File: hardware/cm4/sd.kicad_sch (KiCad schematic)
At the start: 5 parts, among them J13 microSD, U11 AP22804AW5

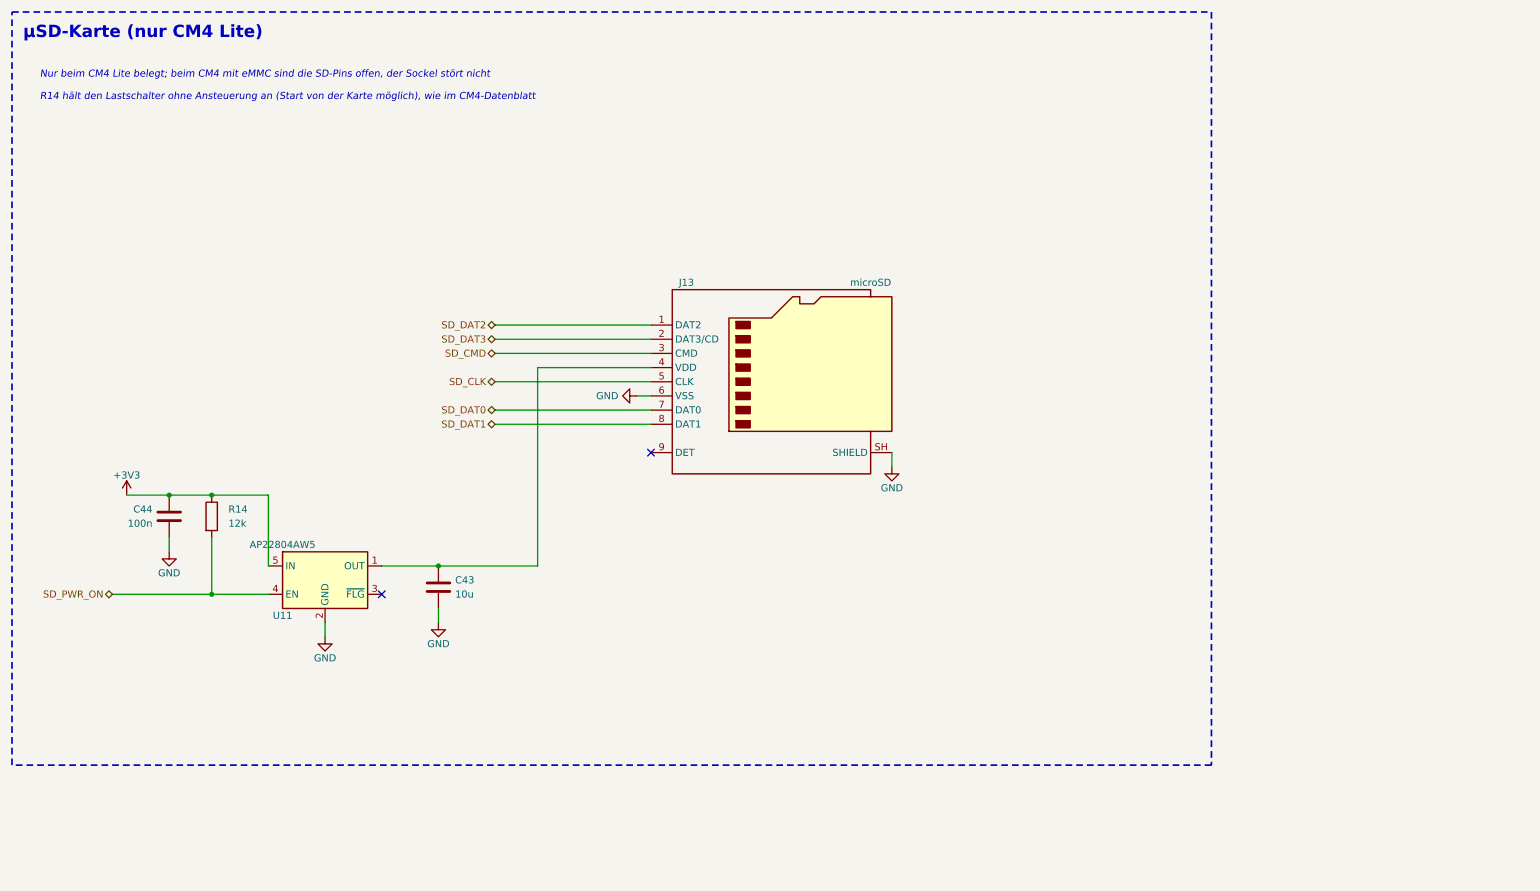
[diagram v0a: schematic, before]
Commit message: CM4-Schaltplan: Einzelblock-Blätter ohne Rahmen, Inhalt zentriert
kicadgen: Steht nur ein Block auf einem Blatt, entfällt der Rahmen (sein Titel wird
Blatttitel) und der Inhalt wird auf dem Blatt zentriert (über dem Schriftfeld, auf dem
1,27-mm-Raster). Hinweistexte der CM4-Blätter an die Schaltungen gerückt.

Co-Authored-By: Claude Opus 5.5 <noreply@anthropic.com>
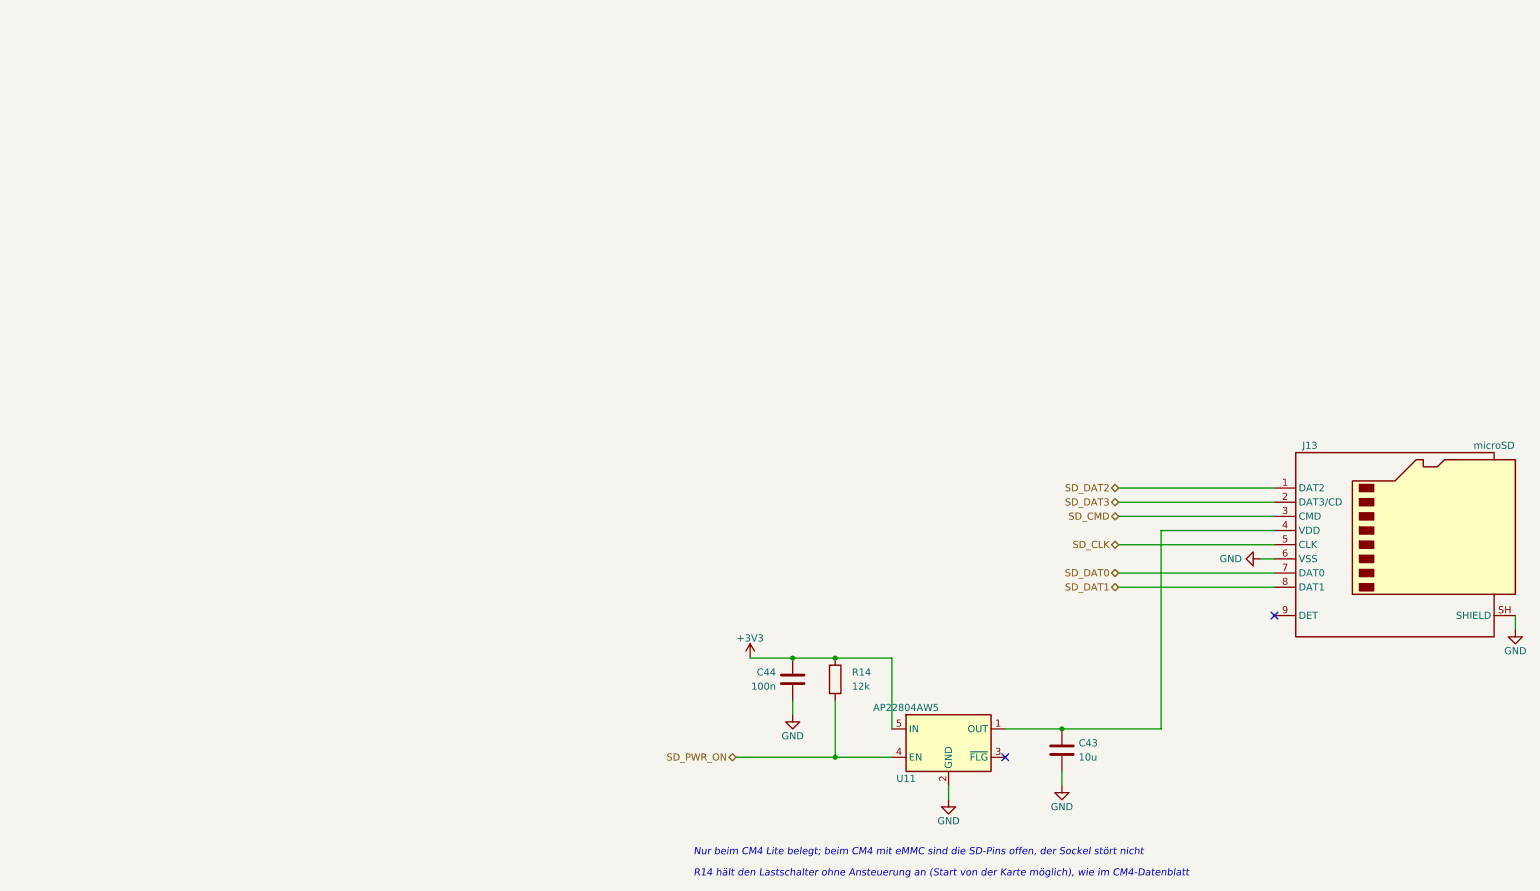
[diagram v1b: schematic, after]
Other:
- note removed: "µSD-Karte (nur CM4 Lite)"
- title: µSD -> µSD-Karte (nur CM4 Lite)
